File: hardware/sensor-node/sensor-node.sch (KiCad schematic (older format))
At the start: 52 parts, among them J1 Conn_Coaxial, J2 Conn_ARM_JTAG_SWD_10, Q1 Q_PMOS_DGS, U1 AAT1217, U2 TPS27081A, U3 SHT31-DIS, U4 24LC32, U5 MLX90614, U6 ADG633YCP, U7 TSV911RILT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

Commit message: Fix timeouts for systick overflow handling
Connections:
- net GND: now also U4.7 (WP)
- no-connect marks 21 -> 20
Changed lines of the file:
@@
 Wire Wire Line
 	9050 2500 9050 2700
-NoConn ~ 8600 2350
 Text GLabel 8600 2150 2    50   Input ~ 0
 SDA
@@
 Text Notes 12300 7400 0    50   ~ 0
 I2C Bus Control
+$Comp
+L power:GND #PWR?
+U 1 1 6002A3D1
+P 8600 2700
+F 0 "#PWR?" H 8600 2450 50  0001 C CNN
+F 1 "GND" H 8605 2527 50  0000 C CNN
+F 2 "" H 8600 2700 50  0001 C CNN
+F 3 "" H 8600 2700 50  0001 C CNN
+	1    8600 2700
+	1    0    0    -1
+$EndComp
+Wire Wire Line
+	8600 2350 8600 2700
 $EndSCHEMATC

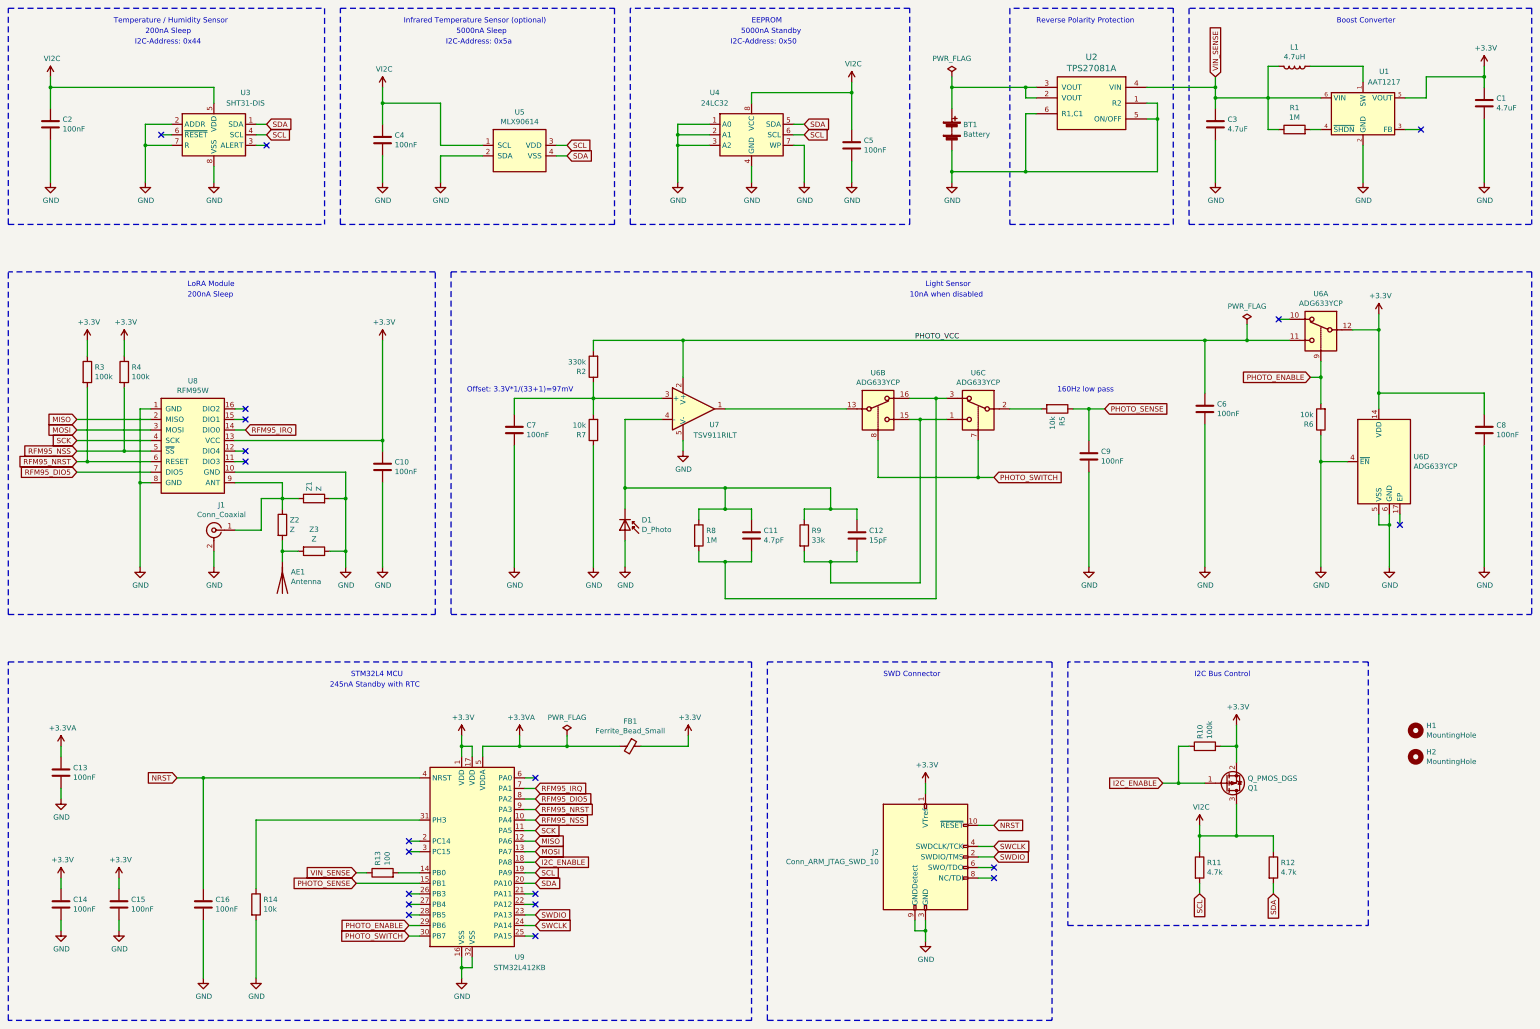
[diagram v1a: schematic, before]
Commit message: Update PCB for enclosure
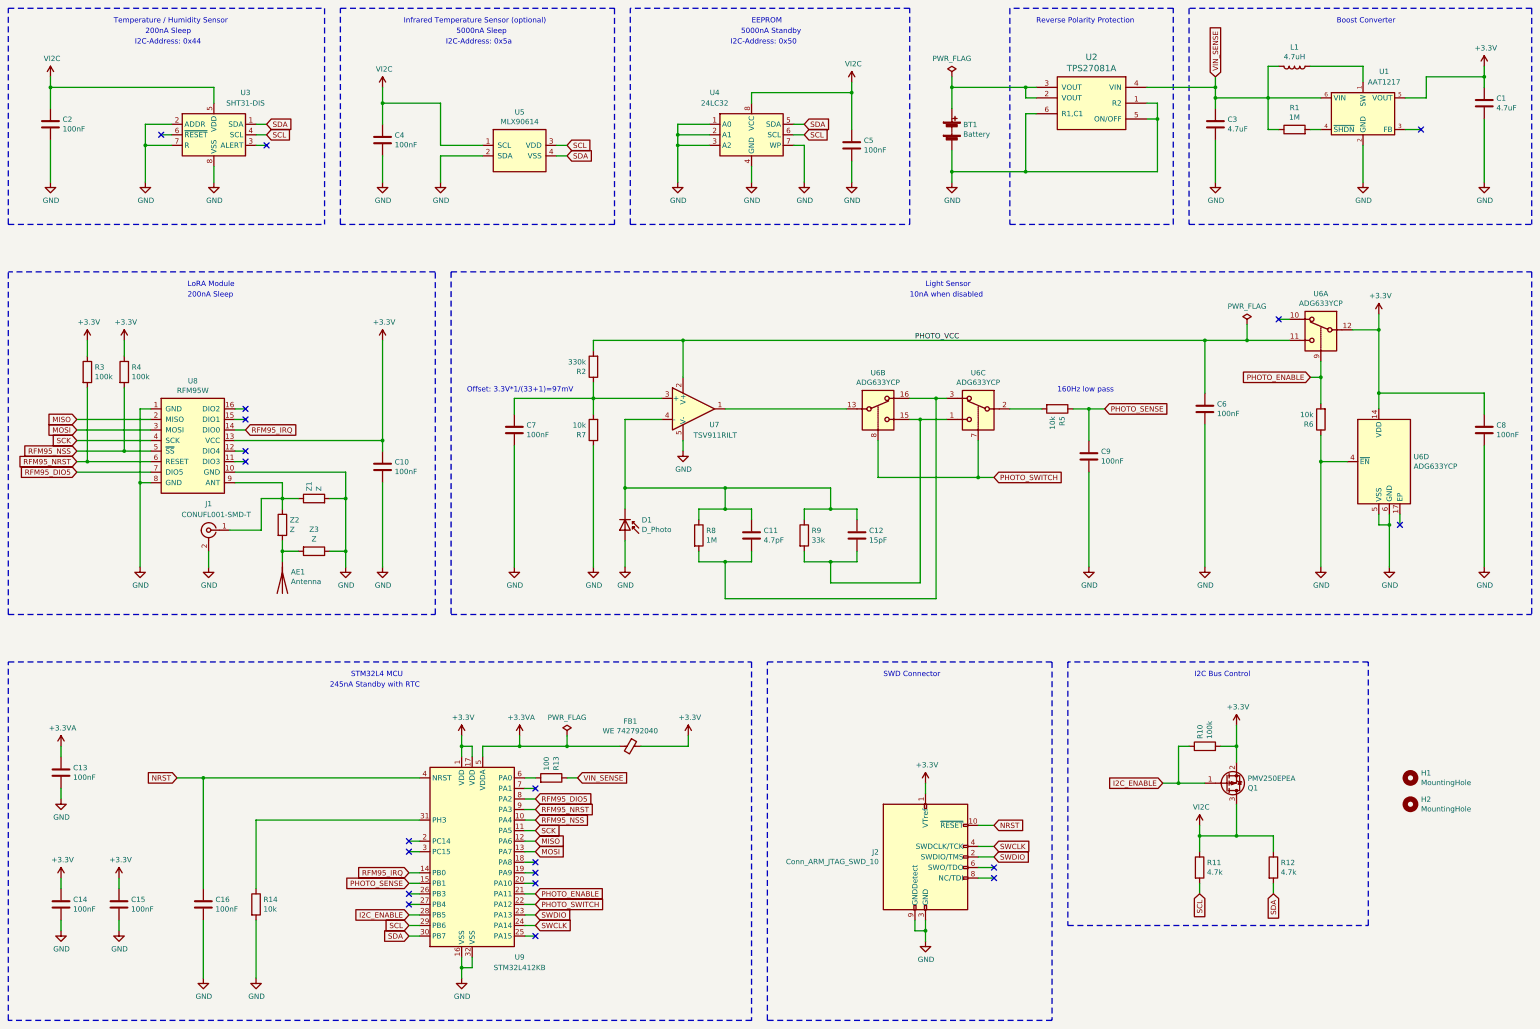
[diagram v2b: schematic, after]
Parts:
- FB1: value Ferrite_Bead_Small -> WE 742792040
- J1: value Conn_Coaxial -> CONUFL001-SMD-T
- J2: footprint my-footprints-library:Amphenol_FCI_ShroudedSocket_2x05_P1.27mm_Vertical_SMD -> my-footprints-library:SHF-105-01-L-D-TH
- Q1: value Q_PMOS_DGS -> PMV250EPEA
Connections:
- net I2C_ENABLE: now also U9.28 (PB5); no longer U9.18 (PA8)
- net PHOTO_ENABLE: now also U9.21 (PA11); no longer U9.29 (PB6)
- net PHOTO_SWITCH: now also U9.22 (PA12); no longer U9.30 (PB7)
- net RFM95_IRQ: now also U9.14 (PB0); no longer U9.7 (PA1)
- net SCL: now also U9.29 (PB6); no longer U9.19 (PA9)
- net SDA: now also U9.30 (PB7); no longer U9.20 (PA10)
- net at R13.2: now also U9.6 (PA0); no longer U9.14 (PB0)
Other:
- moved on the sheet: H1, H2, J1, R13
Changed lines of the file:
@@
 F 0 "J2" H 9307 9146 50  0000 R CNN
 F 1 "Conn_ARM_JTAG_SWD_10" H 9307 9055 50  0000 R CNN
-F 2 "my-footprints-library:Amphenol_FCI_ShroudedSocket_2x05_P1.27mm_Vertical_SMD" H 9750 9100 50  0001 C CNN
+F 2 "my-footprints-library:SHF-105-01-L-D-TH" H 9750 9100 50  0001 C CNN
 F 3 "http://infocenter.arm.com/help/topic/com.arm.doc.ddi0314h/DDI0314H_coresight_components_trm.pdf" V 9400 7850 50  0001 C CNN
 	1    9750 9100
@@
 P 6950 8050
 F 0 "FB1" V 6713 8050 50  0000 C CNN
-F 1 "Ferrite_Bead_Small" V 6804 8050 50  0000 C CNN
+F 1 "WE 742792040" V 6804 8050 50  0000 C CNN
 F 2 "Inductor_SMD:L_0805_2012Metric_Pad1.05x1.20mm_HandSolder" V 6880 8050 50  0001 C CNN
 F 3 "~" H 6950 8050 50  0001 C CNN
@@
 Wire Notes Line
 	1050 7250 8100 7250
-NoConn ~ 4850 9050
-NoConn ~ 4850 8950
 Wire Wire Line
 	4950 9050 4850 9050
@@
 	5950 9150 6050 9150
 Wire Wire Line
-	4350 9350 4950 9350
+	4850 9350 4950 9350
 Wire Wire Line
 	5950 8750 6050 8750
@@
 Wire Wire Line
 	4950 9550 4850 9550
-Text GLabel 6050 9350 2    50   Input ~ 0
+Text GLabel 4850 9850 0    50   Input ~ 0
 SDA
-Text GLabel 6050 9250 2    50   Input ~ 0
+Text GLabel 4850 9750 0    50   Input ~ 0
 SCL
 Wire Wire Line
@@
 Wire Notes Line
 	5250 3550 5250 6800
-Text GLabel 4350 9350 0    50   Input ~ 0
+Text GLabel 4850 9350 0    50   Input ~ 0
 PHOTO_SENSE
-Text GLabel 4850 9850 0    50   Input ~ 0
+Text GLabel 6050 9550 2    50   Input ~ 0
 PHOTO_SWITCH
-Text GLabel 4850 9750 0    50   Input ~ 0
+Text GLabel 6050 9450 2    50   Input ~ 0
 PHOTO_ENABLE
-Text GLabel 6050 8450 2    50   Input ~ 0
+Text GLabel 4850 9250 0    50   Input ~ 0
 RFM95_IRQ
 Text GLabel 6050 8550 2    50   Input ~ 0
 RFM95_DIO5
-Text GLabel 4350 9250 0    50   Input ~ 0
+Text GLabel 6450 8350 2    50   Input ~ 0
 VIN_SENSE
 Connection ~ 5900 8050
@@
 L Mechanical:MountingHole H1
 U 1 1 5FA37933
-P 14400 7900
-F 0 "H1" H 14500 7946 50  0000 L CNN
-F 1 "MountingHole" H 14500 7855 50  0000 L CNN
-F 2 "MountingHole:MountingHole_2.2mm_M2" H 14400 7900 50  0001 C CNN
-F 3 "~" H 14400 7900 50  0001 C CNN
-	1    14400 7900
+P 14350 8350
+F 0 "H1" H 14450 8396 50  0000 L CNN
+F 1 "MountingHole" H 14450 8305 50  0000 L CNN
+F 2 "MountingHole:MountingHole_2.2mm_M2" H 14350 8350 50  0001 C CNN
+F 3 "~" H 14350 8350 50  0001 C CNN
+	1    14350 8350
 	1    0    0    -1
 $EndComp
@@
 L Mechanical:MountingHole H2
 U 1 1 5FA3863F
-P 14400 8150
-F 0 "H2" H 14500 8196 50  0000 L CNN
-F 1 "MountingHole" H 14500 8105 50  0000 L CNN
-F 2 "MountingHole:MountingHole_2.2mm_M2" H 14400 8150 50  0001 C CNN
-F 3 "~" H 14400 8150 50  0001 C CNN
-	1    14400 8150
+P 14350 8600
+F 0 "H2" H 14450 8646 50  0000 L CNN
+F 1 "MountingHole" H 14450 8555 50  0000 L CNN
+F 2 "MountingHole:MountingHole_2.2mm_M2" H 14350 8600 50  0001 C CNN
+F 3 "~" H 14350 8600 50  0001 C CNN
+	1    14350 8600
 	1    0    0    -1
 $EndComp
@@
 Wire Wire Line
 	5950 8350 6050 8350
-NoConn ~ 4850 9450
-NoConn ~ 4850 9550
-NoConn ~ 4850 9650
-NoConn ~ 6050 9850
-NoConn ~ 6050 9550
-NoConn ~ 6050 9450
-NoConn ~ 6050 8350
 $Comp
 L power:PWR_FLAG #FLG02
@@
 L Device:R R13
 U 1 1 5FAFF1B9
-P 4600 9250
-F 0 "R13" H 4670 9296 50  0000 L CNN
-F 1 "100" H 4670 9205 50  0000 L CNN
-F 2 "Resistor_SMD:R_0805_2012Metric_Pad1.15x1.40mm_HandSolder" V 4530 9250 50  0001 C CNN
-F 3 "~" H 4600 9250 50  0001 C CNN
-	1    4600 9250
-	0    -1   -1   0
+P 6200 8350
+F 0 "R13" H 6270 8396 50  0000 L CNN
+F 1 "100" H 6270 8305 50  0000 L CNN
+F 2 "Resistor_SMD:R_0805_2012Metric_Pad1.15x1.40mm_HandSolder" V 6130 8350 50  0001 C CNN
+F 3 "~" H 6200 8350 50  0001 C CNN
+	1    6200 8350
+	0    1    -1   0
 $EndComp
 $Comp
@@
 NRST
 Wire Wire Line
-	4750 9250 4950 9250
-Wire Wire Line
-	4450 9250 4350 9250
+	4850 9250 4950 9250
+Wire Wire Line
+	6350 8350 6450 8350
 Wire Wire Line
 	3200 5550 3650 5550
@@
 Wire Wire Line
 	4600 1800 4600 1950
-Text GLabel 6050 9150 2    50   Input ~ 0
+Text GLabel 4850 9650 0    50   Input ~ 0
 I2C_ENABLE
 $Comp
@@
 P 12600 8400
 F 0 "Q1" H 12806 8446 50  0000 L CNN
-F 1 "Q_PMOS_DGS" H 12806 8355 50  0000 L CNN
+F 1 "PMV250EPEA" H 12806 8355 50  0000 L CNN
 F 2 "Package_TO_SOT_SMD:SOT-23" H 12800 8500 50  0001 C CNN
 F 3 "~" H 12600 8400 50  0001 C CNN
@@
 L Connector:Conn_Coaxial J1
 U 1 1 600181AF
-P 3000 6000
-F 0 "J1" H 2928 6238 50  0000 C CNN
-F 1 "Conn_Coaxial" H 2928 6147 50  0000 C CNN
-F 2 "my-footprints-library:CONUFL001-SMD" H 3000 6000 50  0001 C CNN
-F 3 " ~" H 3000 6000 50  0001 C CNN
-	1    3000 6000
+P 2950 6000
+F 0 "J1" H 2950 6250 50  0000 C CNN
+F 1 "CONUFL001-SMD-T" H 2878 6147 50  0000 C CNN
+F 2 "my-footprints-library:CONUFL001-SMD" H 2950 6000 50  0001 C CNN
+F 3 " ~" H 2950 6000 50  0001 C CNN
+	1    2950 6000
 	-1   0    0    -1
 $EndComp
@@
 L power:GND #PWR023
 U 1 1 60030CB8
-P 3000 6350
-F 0 "#PWR023" H 3000 6100 50  0001 C CNN
-F 1 "GND" H 3005 6177 50  0000 C CNN
-F 2 "" H 3000 6350 50  0001 C CNN
-F 3 "" H 3000 6350 50  0001 C CNN
-	1    3000 6350
-	1    0    0    -1
-$EndComp
-Wire Wire Line
-	3000 6200 3000 6350
+P 2950 6350
+F 0 "#PWR023" H 2950 6100 50  0001 C CNN
+F 1 "GND" H 2955 6177 50  0000 C CNN
+F 2 "" H 2950 6350 50  0001 C CNN
+F 3 "" H 2950 6350 50  0001 C CNN
+	1    2950 6350
+	1    0    0    -1
+$EndComp
+Wire Wire Line
+	2950 6200 2950 6350
 Wire Wire Line
 	3650 5700 3450 5700
@@
 	3450 5700 3450 6000
 Wire Wire Line
-	3450 6000 3200 6000
+	3450 6000 3150 6000
 $Comp
 L my-symbols-library:VI2C #PWR02
@@
 I2C Bus Control
 $Comp
-L power:GND #PWR?
+L power:GND #PWR0101
 U 1 1 6002A3D1
 P 8600 2700
-F 0 "#PWR?" H 8600 2450 50  0001 C CNN
+F 0 "#PWR0101" H 8600 2450 50  0001 C CNN
 F 1 "GND" H 8605 2527 50  0000 C CNN
 F 2 "" H 8600 2700 50  0001 C CNN
@@
 Wire Wire Line
 	8600 2350 8600 2700
+NoConn ~ 6050 9150
+NoConn ~ 6050 8450
+NoConn ~ 6050 9250
+NoConn ~ 6050 9350
+NoConn ~ 6050 9850
+NoConn ~ 4850 9450
+NoConn ~ 4850 9550
+NoConn ~ 4850 8950
+NoConn ~ 4850 9050
 $EndSCHEMATC

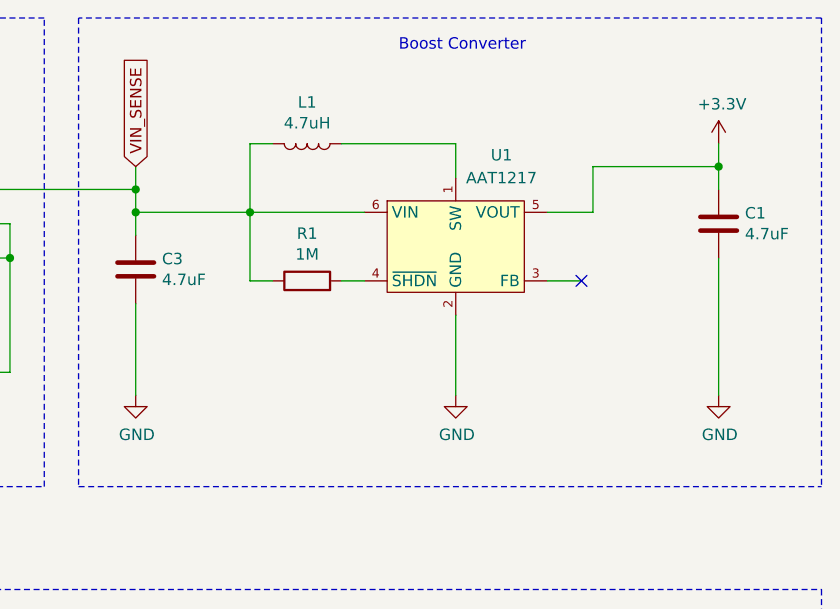
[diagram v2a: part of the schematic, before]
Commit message: Switch to available boost converter
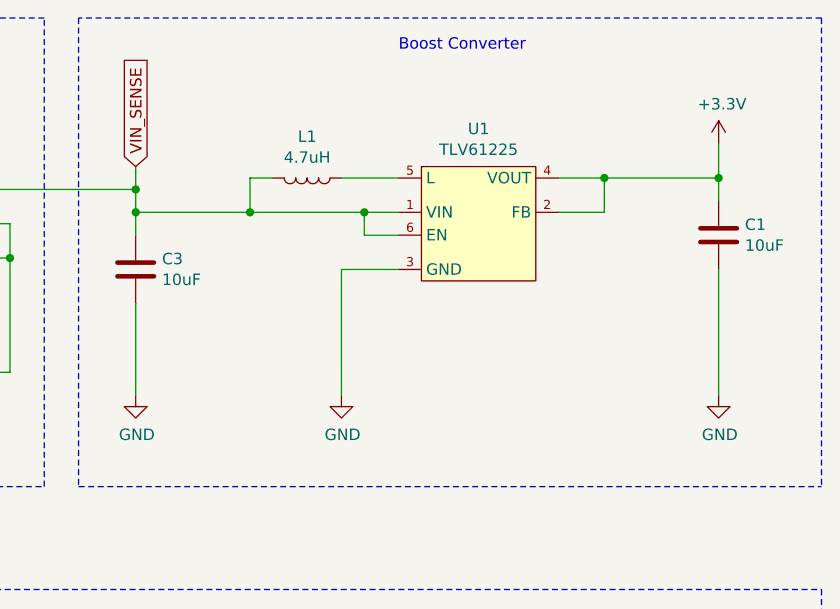
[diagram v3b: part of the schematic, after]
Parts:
- removed R1: 1M, Resistor_SMD:R_0805_2012Metric_Pad1.20x1.40mm_HandSolder, symbol Device:R
- removed U1: AAT1217, Package_TO_SOT_SMD:TSOT-23-6, symbol my-symbols-library:AAT1217
- added U1: TLV61225, Package_TO_SOT_SMD:TSOT-23-6, symbol my-symbols-library:TLV61225
- C1, C3: value 4.7uF -> 10uF
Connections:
- net +3V3: now also U1.2 (FB), U1.4 (VOUT)
- net GND: now also U1.3 (GND)
- net VIN_SENSE: now also U1.1 (VIN), U1.6 (EN)
- net at L1.1: now also U1.5 (L)
- no-connect marks 20 -> 19
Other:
- moved on the sheet: C1, L1
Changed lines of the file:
@@
 $EndDescr
-$Comp
-L Device:R R1
-U 1 1 5F915A91
-P 13250 2200
-F 0 "R1" V 13457 2200 50  0000 C CNN
-F 1 "1M" V 13366 2200 50  0000 C CNN
-F 2 "Resistor_SMD:R_0805_2012Metric_Pad1.20x1.40mm_HandSolder" V 13180 2200 50  0001 C CNN
-F 3 "~" H 13250 2200 50  0001 C CNN
-	1    13250 2200
-	0    -1   -1   0
-$EndComp
 $Comp
 L Device:C C3
@@
 P 12500 2150
 F 0 "C3" H 12615 2196 50  0000 L CNN
-F 1 "4.7uF" H 12615 2105 50  0000 L CNN
+F 1 "10uF" H 12615 2105 50  0000 L CNN
 F 2 "Capacitor_SMD:C_0805_2012Metric_Pad1.18x1.45mm_HandSolder" H 12538 2000 50  0001 C CNN
 F 3 "~" H 12500 2150 50  0001 C CNN
@@
 L Device:C C1
 U 1 1 5F915A9D
-P 15050 1950
-F 0 "C1" H 15165 1996 50  0000 L CNN
-F 1 "4.7uF" H 15165 1905 50  0000 L CNN
-F 2 "Capacitor_SMD:C_0805_2012Metric_Pad1.18x1.45mm_HandSolder" H 15088 1800 50  0001 C CNN
-F 3 "~" H 15050 1950 50  0001 C CNN
-	1    15050 1950
+P 15050 2000
+F 0 "C1" H 15165 2046 50  0000 L CNN
+F 1 "10uF" H 15165 1955 50  0000 L CNN
+F 2 "Capacitor_SMD:C_0805_2012Metric_Pad1.18x1.45mm_HandSolder" H 15088 1850 50  0001 C CNN
+F 3 "~" H 15050 2000 50  0001 C CNN
+	1    15050 2000
 	1    0    0    -1
 $EndComp
@@
 L Device:L L1
 U 1 1 5F915AA3
-P 13250 1600
-F 0 "L1" V 13069 1600 50  0000 C CNN
-F 1 "4.7uH" V 13160 1600 50  0000 C CNN
-F 2 "my-footprints-library:L_Bourns-SRN4018_With3DModel" H 13250 1600 50  0001 C CNN
-F 3 "~" H 13250 1600 50  0001 C CNN
-	1    13250 1600
+P 13250 1750
+F 0 "L1" V 13069 1750 50  0000 C CNN
+F 1 "4.7uH" V 13160 1750 50  0000 C CNN
+F 2 "my-footprints-library:L_Bourns-SRN4018_With3DModel" H 13250 1750 50  0001 C CNN
+F 3 "~" H 13250 1750 50  0001 C CNN
+	1    13250 1750
 	0    1    1    0
 $EndComp
-Wire Wire Line
-	13500 2200 13400 2200
-Wire Wire Line
-	13500 1900 13000 1900
-Wire Wire Line
-	13100 2200 13000 2200
-Wire Wire Line
-	13000 2200 13000 1900
 Connection ~ 13000 1900
 Wire Wire Line
-	13400 1600 13900 1600
-Wire Wire Line
-	13900 1600 13900 1750
-Wire Wire Line
-	13100 1600 13000 1600
-Wire Wire Line
-	13000 1600 13000 1900
+	13100 1750 13000 1750
+Wire Wire Line
+	13000 1750 13000 1900
 Wire Wire Line
 	12500 2000 12500 1900
@@
 Connection ~ 12500 1900
 Wire Wire Line
-	14300 1900 14500 1900
-Wire Wire Line
-	14500 1900 14500 1700
-Wire Wire Line
-	15050 1700 15050 1800
-Wire Wire Line
-	15050 2100 15050 2700
+	15050 1750 15050 1850
+Wire Wire Line
+	15050 2150 15050 2700
 Wire Wire Line
 	12500 2300 12500 2700
@@
 L power:GND #PWR015
 U 1 1 5F915AC9
-P 13900 2700
-F 0 "#PWR015" H 13900 2450 50  0001 C CNN
-F 1 "GND" H 13905 2527 50  0000 C CNN
-F 2 "" H 13900 2700 50  0001 C CNN
-F 3 "" H 13900 2700 50  0001 C CNN
-	1    13900 2700
+P 13400 2700
+F 0 "#PWR015" H 13400 2450 50  0001 C CNN
+F 1 "GND" H 13405 2527 50  0000 C CNN
+F 2 "" H 13400 2700 50  0001 C CNN
+F 3 "" H 13400 2700 50  0001 C CNN
+	1    13400 2700
 	1    0    0    -1
 $EndComp
@@
 $EndComp
 Wire Wire Line
-	13900 2700 13900 2350
-Wire Wire Line
-	15050 1700 15050 1600
-Connection ~ 15050 1700
+	15050 1750 15050 1600
+Connection ~ 15050 1750
 Wire Wire Line
 	12500 1900 12500 1800
@@
 F 3 "" H 10000 2700 50  0001 C CNN
 	1    10000 2700
-	1    0    0    -1
-$EndComp
-$Comp
-L my-symbols-library:AAT1217 U1
-U 1 1 5F915AED
-P 13900 1750
-F 0 "U1" H 14100 1850 50  0000 C CNN
-F 1 "AAT1217" H 14100 1750 50  0000 C CNN
-F 2 "Package_TO_SOT_SMD:TSOT-23-6" H 13900 1500 60  0001 C CNN
-F 3 "" H 13300 1150 60  0001 C CNN
-	1    13900 1750
 	1    0    0    -1
 $EndComp
@@
 Wire Wire Line
 	2600 2250 2500 2250
-Wire Wire Line
-	14500 1700 15050 1700
-Wire Wire Line
-	14300 2200 14450 2200
-NoConn ~ 14450 2200
 Wire Wire Line
 	5900 8050 6350 8050
@@
 NoConn ~ 4850 8950
 NoConn ~ 4850 9050
+$Comp
+L my-symbols-library:TLV61225 U1
+U 1 1 5FC5F2C0
+P 14000 2000
+F 0 "U1" H 14000 2465 50  0000 C CNN
+F 1 "TLV61225" H 14000 2374 50  0000 C CNN
+F 2 "Package_TO_SOT_SMD:TSOT-23-6" H 14000 2100 60  0001 C CNN
+F 3 "" H 13400 1400 60  0001 C CNN
+	1    14000 2000
+	1    0    0    -1
+$EndComp
+Wire Wire Line
+	13650 1750 13400 1750
+Wire Wire Line
+	13000 1900 13500 1900
+Wire Wire Line
+	13650 2000 13500 2000
+Wire Wire Line
+	13500 2000 13500 1900
+Connection ~ 13500 1900
+Wire Wire Line
+	13500 1900 13650 1900
+Wire Wire Line
+	13650 2150 13400 2150
+Wire Wire Line
+	13400 2150 13400 2700
+Wire Wire Line
+	14350 1750 14550 1750
+Wire Wire Line
+	14350 1900 14550 1900
+Wire Wire Line
+	14550 1900 14550 1750
+Connection ~ 14550 1750
+Wire Wire Line
+	14550 1750 15050 1750
 $EndSCHEMATC
